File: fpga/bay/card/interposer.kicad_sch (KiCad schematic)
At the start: 1 part, among them J1 FXBeam_2x74_DB

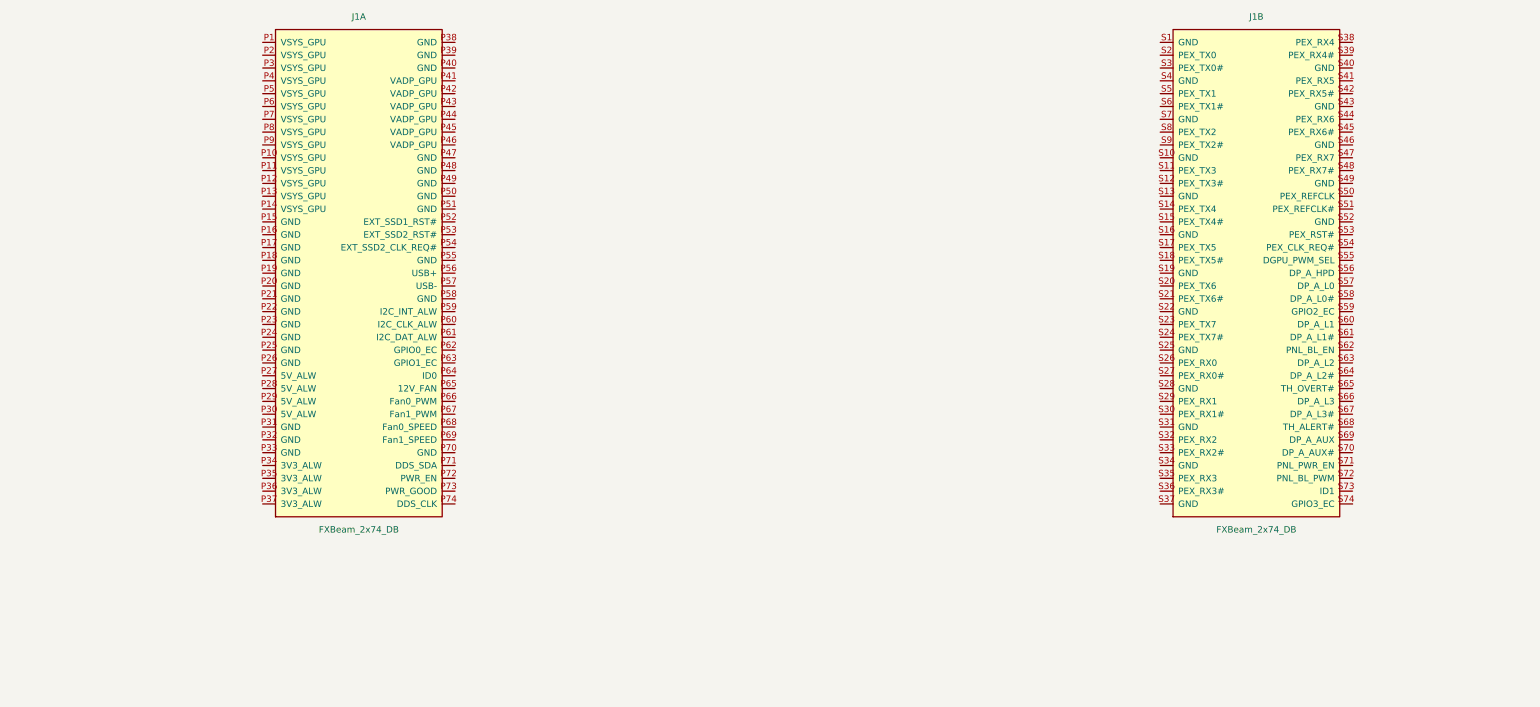
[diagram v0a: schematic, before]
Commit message: Phase 2 path2: wire interposer sheet (J1 global labels, ID0/ID1 330k, NC, PWR_FLAGs)
Co-Authored-By: Claude Opus 5.5 <noreply@anthropic.com>
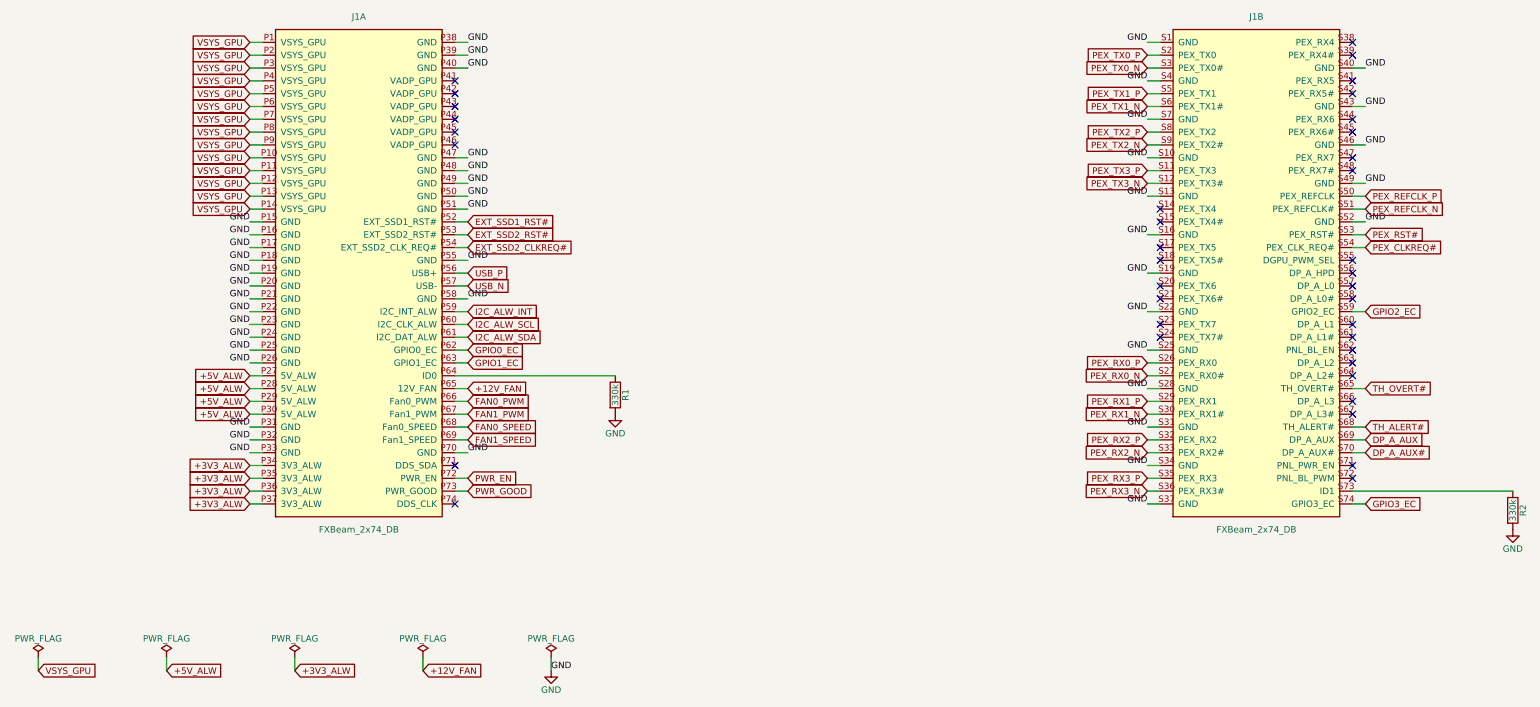
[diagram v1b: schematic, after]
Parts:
- added R1, R2: 330k, Resistor_SMD:R_0402_1005Metric, symbol Device:R
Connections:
- net VSYS_GPU: now reaches J1.P1 (VSYS_GPU)
- net VSYS_GPU: now also J1.P10 (VSYS_GPU), J1.P11 (VSYS_GPU), J1.P12 (VSYS_GPU), J1.P13 (VSYS_GPU), J1.P14 (VSYS_GPU), J1.P2 (VSYS_GPU), J1.P3 (VSYS_GPU), J1.P4 (VSYS_GPU), J1.P5 (VSYS_GPU), J1.P6 (VSYS_GPU), J1.P7 (VSYS_GPU), J1.P8 (VSYS_GPU), J1.P9 (VSYS_GPU)
- net GND: now reaches J1.P15 (GND)
- net GND: now also J1.P16 (GND), J1.P17 (GND), J1.P18 (GND), J1.P19 (GND), J1.P20 (GND), J1.P21 (GND), J1.P22 (GND), J1.P23 (GND), J1.P24 (GND), J1.P25 (GND), J1.P26 (GND), J1.P31 (GND), J1.P32 (GND), J1.P33 (GND), J1.P38 (GND), J1.P39 (GND), J1.P40 (GND), J1.P47 (GND), J1.P48 (GND), J1.P49 (GND), J1.P50 (GND), J1.P51 (GND), J1.P55 (GND), J1.P58 (GND), J1.P70 (GND), J1.S1 (GND), J1.S10 (GND), J1.S13 (GND), J1.S16 (GND), J1.S19 (GND), J1.S22 (GND), J1.S25 (GND), J1.S28 (GND), J1.S31 (GND), J1.S34 (GND), J1.S37 (GND), J1.S4 (GND), J1.S40 (GND), J1.S43 (GND), J1.S46 (GND), J1.S49 (GND), J1.S52 (GND), J1.S7 (GND), R1.2, R2.2
- net +5V_ALW: now reaches J1.P27 (5V_ALW)
- net +5V_ALW: now also J1.P28 (5V_ALW), J1.P29 (5V_ALW), J1.P30 (5V_ALW)
- net +3V3_ALW: now reaches J1.P34 (3V3_ALW)
- net +3V3_ALW: now also J1.P35 (3V3_ALW), J1.P36 (3V3_ALW), J1.P37 (3V3_ALW)
- net EXT_SSD1_RST#: now reaches J1.P52 (EXT_SSD1_RST#)
- net EXT_SSD2_RST#: now reaches J1.P53 (EXT_SSD2_RST#)
- net EXT_SSD2_CLKREQ#: now reaches J1.P54 (EXT_SSD2_CLK_REQ#)
- net USB_P: now reaches J1.P56 (USB+)
- net USB_N: now reaches J1.P57 (USB-)
- net I2C_ALW_INT: now reaches J1.P59 (I2C_INT_ALW)
- net I2C_ALW_SCL: now reaches J1.P60 (I2C_CLK_ALW)
- net I2C_ALW_SDA: now reaches J1.P61 (I2C_DAT_ALW)
- net GPIO0_EC: now reaches J1.P62 (GPIO0_EC)
- net GPIO1_EC: now reaches J1.P63 (GPIO1_EC)
- net at J1.P64 (ID0): now also R1.1
- net +12V_FAN: now reaches J1.P65 (12V_FAN)
- net FAN0_PWM: now reaches J1.P66 (Fan0_PWM)
- net FAN1_PWM: now reaches J1.P67 (Fan1_PWM)
- net FAN0_SPEED: now reaches J1.P68 (Fan0_SPEED)
- net FAN1_SPEED: now reaches J1.P69 (Fan1_SPEED)
- net PWR_EN: now reaches J1.P72 (PWR_EN)
- net PWR_GOOD: now reaches J1.P73 (PWR_GOOD)
- net PEX_TX3_P: now reaches J1.S11 (PEX_TX3)
- net PEX_TX3_N: now reaches J1.S12 (PEX_TX3#)
- net PEX_TX0_P: now reaches J1.S2 (PEX_TX0)
- net PEX_RX0_P: now reaches J1.S26 (PEX_RX0)
- net PEX_RX0_N: now reaches J1.S27 (PEX_RX0#)
- net PEX_RX1_P: now reaches J1.S29 (PEX_RX1)
- net PEX_TX0_N: now reaches J1.S3 (PEX_TX0#)
- net PEX_RX1_N: now reaches J1.S30 (PEX_RX1#)
- net PEX_RX2_P: now reaches J1.S32 (PEX_RX2)
- net PEX_RX2_N: now reaches J1.S33 (PEX_RX2#)
- net PEX_RX3_P: now reaches J1.S35 (PEX_RX3)
- net PEX_RX3_N: now reaches J1.S36 (PEX_RX3#)
- net PEX_TX1_P: now reaches J1.S5 (PEX_TX1)
- net PEX_REFCLK_P: now reaches J1.S50 (PEX_REFCLK)
- net PEX_REFCLK_N: now reaches J1.S51 (PEX_REFCLK#)
- net PEX_RST#: now reaches J1.S53 (PEX_RST#)
- net PEX_CLKREQ#: now reaches J1.S54 (PEX_CLK_REQ#)
- net GPIO2_EC: now reaches J1.S59 (GPIO2_EC)
- net PEX_TX1_N: now reaches J1.S6 (PEX_TX1#)
- net TH_OVERT#: now reaches J1.S65 (TH_OVERT#)
- net TH_ALERT#: now reaches J1.S68 (TH_ALERT#)
- net DP_A_AUX: now reaches J1.S69 (DP_A_AUX)
- net DP_A_AUX#: now reaches J1.S70 (DP_A_AUX#)
- net at J1.S73 (ID1): now also R2.1
- net GPIO3_EC: now reaches J1.S74 (GPIO3_EC)
- net PEX_TX2_P: now reaches J1.S8 (PEX_TX2)
- net PEX_TX2_N: now reaches J1.S9 (PEX_TX2#)
- no-connect marks 0 -> 37

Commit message: fpga: rename KiCad project and library omnimeter-card/omnimeter -> fw16-fpga-module
Co-Authored-By: Claude Opus 5.5 (1M context) <noreply@anthropic.com>
Claude-Session: https://claude.ai/code/session_019QA2U79cSHCaAaMe6Km575
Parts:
- J1: footprint omnimeter:FXBeam_2x74_DB -> fw16-fpga-module:FXBeam_2x74_DB; symbol omnimeter:FXBeam_2x74_DB -> fw16-fpga-module:FXBeam_2x74_DB
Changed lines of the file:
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@@
 	)
 	(symbol
-		(lib_id "omnimeter:FXBeam_2x74_DB")
+		(lib_id "fw16-fpga-module:FXBeam_2x74_DB")
 		(at 101.6 152.4 0)
 		(unit 1)
@@
 			)
 		)
-		(property "Footprint" "omnimeter:FXBeam_2x74_DB"
+		(property "Footprint" "fw16-fpga-module:FXBeam_2x74_DB"
 			(at 101.6 152.4 0)
 			(hide yes)
@@
 		)
 		(instances
-			(project "omnimeter-card"
+			(project "fw16-fpga-module"
 				(path "/d7dcd351-036e-417b-86ff-4ba43184a562/19ac7f60-146c-4f0e-8f0b-4db8f2252d97"
 					(reference "J1")
@@
 	)
 	(symbol
-		(lib_id "omnimeter:FXBeam_2x74_DB")
+		(lib_id "fw16-fpga-module:FXBeam_2x74_DB")
 		(at 279.4 152.4 0)
 		(unit 2)
@@
 			)
 		)
-		(property "Footprint" "omnimeter:FXBeam_2x74_DB"
+		(property "Footprint" "fw16-fpga-module:FXBeam_2x74_DB"
 			(at 279.4 152.4 0)
 			(hide yes)
@@
 		)
 		(instances
-			(project "omnimeter-card"
+			(project "fw16-fpga-module"
 				(path "/d7dcd351-036e-417b-86ff-4ba43184a562/19ac7f60-146c-4f0e-8f0b-4db8f2252d97"
 					(reference "J1")
@@
 		)
 		(instances
-			(project "omnimeter-card"
+			(project "fw16-fpga-module"
 				(path "/d7dcd351-036e-417b-86ff-4ba43184a562/19ac7f60-146c-4f0e-8f0b-4db8f2252d97"
 					(reference "R1")
@@
 		)
 		(instances
-			(project "omnimeter-card"
+			(project "fw16-fpga-module"
 				(path "/d7dcd351-036e-417b-86ff-4ba43184a562/19ac7f60-146c-4f0e-8f0b-4db8f2252d97"
 					(reference "R2")
@@
 		)
 		(instances
-			(project "omnimeter-card"
+			(project "fw16-fpga-module"
 				(path "/d7dcd351-036e-417b-86ff-4ba43184a562/19ac7f60-146c-4f0e-8f0b-4db8f2252d97"
 					(reference "#FLG01")
@@
 		)
 		(instances
-			(project "omnimeter-card"
+			(project "fw16-fpga-module"
 				(path "/d7dcd351-036e-417b-86ff-4ba43184a562/19ac7f60-146c-4f0e-8f0b-4db8f2252d97"
 					(reference "#FLG02")
@@
 		)
 		(instances
-			(project "omnimeter-card"
+			(project "fw16-fpga-module"
 				(path "/d7dcd351-036e-417b-86ff-4ba43184a562/19ac7f60-146c-4f0e-8f0b-4db8f2252d97"
 					(reference "#FLG03")
@@
 		)
 		(instances
-			(project "omnimeter-card"
+			(project "fw16-fpga-module"
 				(path "/d7dcd351-036e-417b-86ff-4ba43184a562/19ac7f60-146c-4f0e-8f0b-4db8f2252d97"
 					(reference "#FLG04")
@@
 		)
 		(instances
-			(project "omnimeter-card"
+			(project "fw16-fpga-module"
 				(path "/d7dcd351-036e-417b-86ff-4ba43184a562/19ac7f60-146c-4f0e-8f0b-4db8f2252d97"
 					(reference "#FLG05")
@@
 		)
 		(instances
-			(project "omnimeter-card"
+			(project "fw16-fpga-module"
 				(path "/d7dcd351-036e-417b-86ff-4ba43184a562/19ac7f60-146c-4f0e-8f0b-4db8f2252d97"
 					(reference "#PWR01")
@@
 		)
 		(instances
-			(project "omnimeter-card"
+			(project "fw16-fpga-module"
 				(path "/d7dcd351-036e-417b-86ff-4ba43184a562/19ac7f60-146c-4f0e-8f0b-4db8f2252d97"
 					(reference "#PWR02")
@@
 		)
 		(instances
-			(project "omnimeter-card"
+			(project "fw16-fpga-module"
 				(path "/d7dcd351-036e-417b-86ff-4ba43184a562/19ac7f60-146c-4f0e-8f0b-4db8f2252d97"
 					(reference "#PWR03")
